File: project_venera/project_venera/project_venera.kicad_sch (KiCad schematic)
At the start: 10 parts, among them IC1 NCV303LSN11T1G, IC2 TC1262-3.3VDBTR, IC3 ATSAMD11D14A-SSUT

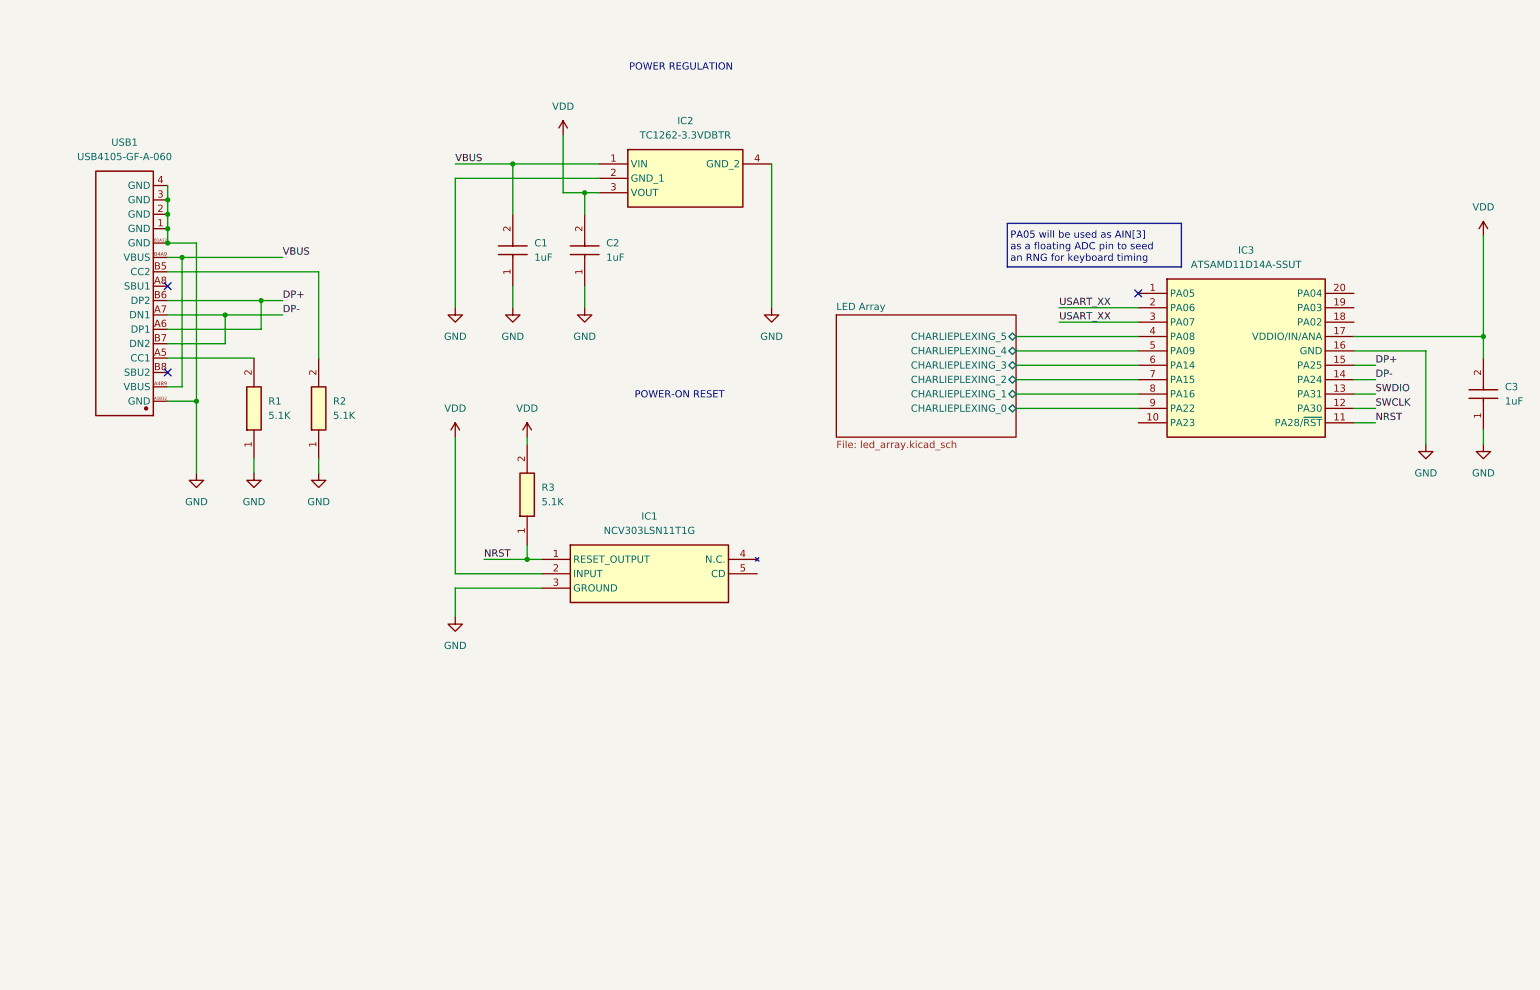
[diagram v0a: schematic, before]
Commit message: update main schematic page, add buttons, gpio pins
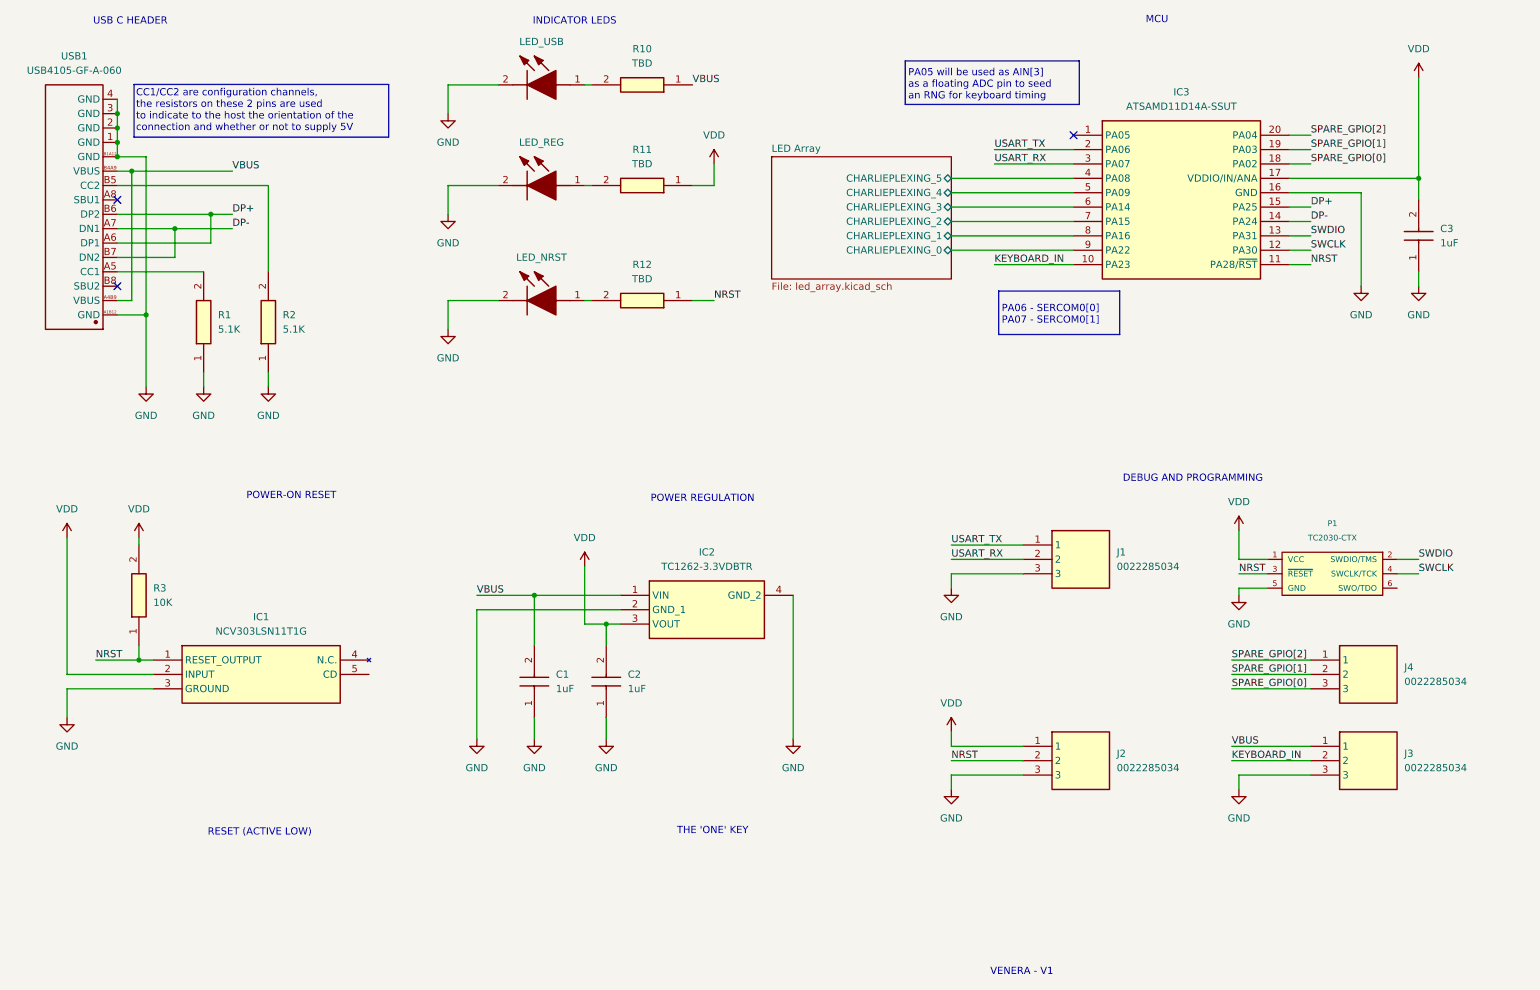
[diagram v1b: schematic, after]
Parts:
- added J1, J2, J3, J4: 0022285034, 0022285034, symbol LibraryLoader:0022285034
- added LED_NRST, LED_REG, LED_USB: SM0603SRC, SM0603SRC, symbol LibraryLoader:SM0603SRC
- added P1: TC2030-CTX, TagConnect:TC2030_SMALL, symbol TagConnect:TC2030-CTX
- added R10, R11, R12: TBD, LibraryLoader:ERJPC3D9763V, symbol LibraryLoader:ERJ-PC3B4702V
- R3: value 5.1K -> 10K
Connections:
- net GND: now also J1.3, J2.3, J3.3, LED_NRST.2 (K), LED_REG.2 (K), LED_USB.2 (K), P1.5 (GND)
- net NRST: now also J2.2, P1.3 (~{RESET}), R12.1
- net SWCLK: now also P1.4 (SWCLK/TCK)
- net SWDIO: now also P1.2 (SWDIO/TMS)
- net VBUS: now also J3.1, R10.1
- net VDD: now also J2.1, P1.1 (VCC), R11.1
- net KEYBOARD_IN: now reaches IC3.10 (PA23)
- net KEYBOARD_IN: now also J3.2
- net SPARE_GPIO[0]: now reaches IC3.18 (PA02)
- net SPARE_GPIO[0]: now also J4.3
- net SPARE_GPIO[1]: now reaches IC3.19 (PA03)
- net SPARE_GPIO[1]: now also J4.2
- net SPARE_GPIO[2]: now reaches IC3.20 (PA04)
- net SPARE_GPIO[2]: now also J4.1
- net USART_XX renamed USART_RX
- net USART_RX: now also J1.2; no longer IC3.2 (PA06)
- new net: LED_REG.1 (A), R11.2
- new net: LED_USB.1 (A), R10.2
- new net: LED_NRST.1 (A), R12.2
- new net USART_TX: IC3.2 (PA06), J1.1
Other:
- note added: "CC1/CC2 are configuration channels, the resistors on these 2 pins are used to indicate to the host the orientation of the connection and whether or not to supply 5V"
- note added: "DEBUG AND PROGRAMMING"
- note added: "INDICATOR LEDS"
- note added: "MCU"
- note added: "PA06 - SERCOM0[0] PA07 - SERCOM0[1]"
- note added: "RESET (ACTIVE LOW)"
- note added: "THE 'ONE' KEY"
- note added: "USB C HEADER"
- note added: "VENERA - V1"
- moved on the sheet: C1, C2, C3, IC1, IC2, IC3, R1, R2, R3, USB1
